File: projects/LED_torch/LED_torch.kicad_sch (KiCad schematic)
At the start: 4 parts, among them SW1 SW_DPDT_x2

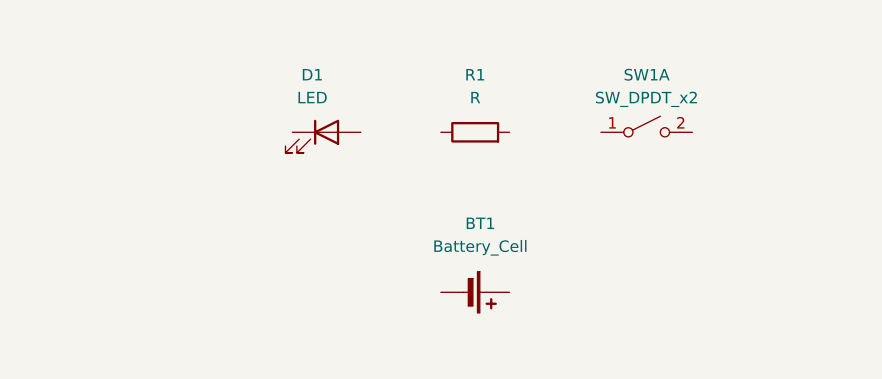
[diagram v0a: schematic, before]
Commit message: Project 1-LED Torch v01 v02 v03 and logos
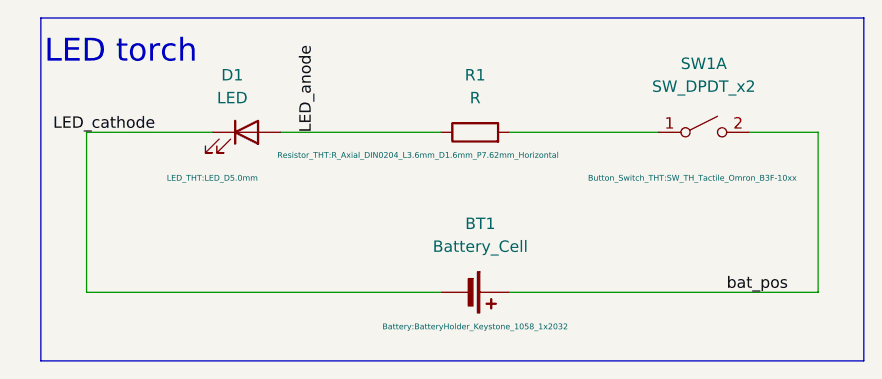
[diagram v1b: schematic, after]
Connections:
- net LED_anode: now reaches R1.1
- net LED_anode: now also D1.2 (A)
- net at R1.2: now also SW1.1 (A)
- net bat_pos: now reaches BT1.1 (+)
- net bat_pos: now also SW1.2 (B)
- net LED_cathode: now reaches BT1.2 (-)
- net LED_cathode: now also D1.1 (K)
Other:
- note added: "LED torch"
- moved on the sheet: D1, SW1A
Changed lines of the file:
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@@
 	(title_block
 		(title "LED Torch")
-		(date "2025-07-03")
+		(date "2025-07-05")
 		(rev "0.1")
 		(company "Sevillabot")
 		(comment 1 "Project 1 ")
 		(comment 2 "KiCAD like a Pro - Udemy Course")
-		(comment 3 "A basic PBC project")
+		(comment 3 "A basic PCB project")
+	)
+	(rectangle
+		(start 76.2 71.12)
+		(end 167.64 109.22)
+		(stroke
+			(width 0)
+			(type default)
+		)
+		(fill
+			(type none)
+		)
+	)
+	(text "LED torch"
+		(exclude_from_sim no)
+		(at 85.09 74.93 0)
+		(effects
+			(font
+				(face "Lato Black")
+				(size 2.54 2.54)
+			)
+		)
+	)
+	(wire
+		(pts
+			(xy 102.87 83.82) (xy 120.65 83.82)
+		)
+		(stroke
+			(width 0)
+			(type default)
+		)
+	)
+	(wire
+		(pts
+			(xy 81.28 83.82) (xy 95.25 83.82)
+		)
+		(stroke
+			(width 0)
+			(type default)
+		)
+	)
+	(wire
+		(pts
+			(xy 162.56 101.6) (xy 162.56 83.82)
+		)
+		(stroke
+			(width 0)
+			(type default)
+		)
+	)
+	(wire
+		(pts
+			(xy 128.27 83.82) (xy 144.78 83.82)
+		)
+		(stroke
+			(width 0)
+			(type default)
+		)
+	)
+	(wire
+		(pts
+			(xy 128.27 101.6) (xy 162.56 101.6)
+		)
+		(stroke
+			(width 0)
+			(type default)
+		)
+	)
+	(wire
+		(pts
+			(xy 162.56 83.82) (xy 154.94 83.82)
+		)
+		(stroke
+			(width 0)
+			(type default)
+		)
+	)
+	(wire
+		(pts
+			(xy 81.28 101.6) (xy 120.65 101.6)
+		)
+		(stroke
+			(width 0)
+			(type default)
+		)
+	)
+	(wire
+		(pts
+			(xy 81.28 83.82) (xy 81.28 101.6)
+		)
+		(stroke
+			(width 0)
+			(type default)
+		)
+	)
+	(label "LED_cathode"
+		(at 88.9 83.82 180)
+		(effects
+			(font
+				(size 1.27 1.27)
+			)
+			(justify right bottom)
+		)
+	)
+	(label "LED_anode"
+		(at 106.68 83.82 90)
+		(effects
+			(font
+				(size 1.27 1.27)
+			)
+			(justify left bottom)
+		)
+	)
+	(label "bat_pos"
+		(at 152.4 101.6 0)
+		(effects
+			(font
+				(size 1.27 1.27)
+			)
+			(justify left bottom)
+		)
 	)
 	(symbol
@@
 		(on_board yes)
 		(dnp no)
-		(fields_autoplaced yes)
 		(property "Reference" "R1"
 			(at 124.46 77.47 90)
@@
 		)
 		(property "Footprint" "Resistor_THT:R_Axial_DIN0204_L3.6mm_D1.6mm_P7.62mm_Horizontal"
-			(at 124.46 85.598 90)
-			(effects
-				(font
-					(size 1.27 1.27)
-				)
-				(hide yes)
+			(at 118.11 86.36 90)
+			(effects
+				(font
+					(face "Courier 10 Pitch")
+					(size 0.64 0.64)
+				)
 			)
 		)
@@
 		(on_board yes)
 		(dnp no)
-		(fields_autoplaced yes)
 		(property "Reference" "BT1"
 			(at 125.0315 93.98 90)
@@
 		)
 		(property "Footprint" "Battery:BatteryHolder_Keystone_1058_1x2032"
-			(at 124.714 101.6 90)
-			(effects
-				(font
-					(size 1.27 1.27)
-				)
-				(hide yes)
+			(at 124.46 105.41 90)
+			(effects
+				(font
+					(face "Courier 10 Pitch")
+					(size 0.64 0.64)
+				)
 			)
 		)
@@
 	(symbol
 		(lib_id "Switch:SW_DPST_x2")
-		(at 143.51 83.82 0)
+		(at 149.86 83.82 0)
 		(unit 1)
 		(exclude_from_sim no)
@@
 		(on_board yes)
 		(dnp no)
-		(fields_autoplaced yes)
 		(property "Reference" "SW1"
-			(at 143.51 77.47 0)
+			(at 149.86 76.2 0)
 			(effects
 				(font
@@
 		)
 		(property "Value" "SW_DPDT_x2"
-			(at 143.51 80.01 0)
+			(at 149.86 78.74 0)
 			(effects
 				(font
@@
 		)
 		(property "Footprint" "Button_Switch_THT:SW_TH_Tactile_Omron_B3F-10xx"
-			(at 143.51 83.82 0)
-			(effects
-				(font
-					(size 1.27 1.27)
-				)
-				(hide yes)
+			(at 148.59 88.9 0)
+			(effects
+				(font
+					(face "Courier 10 Pitch")
+					(size 0.64 0.64)
+				)
 			)
 		)
 		(property "Datasheet" "~"
-			(at 143.51 83.82 0)
+			(at 149.86 83.82 0)
 			(effects
 				(font
@@
 		)
 		(property "Description" "Single Pole Single Throw (SPST) switch, separate symbol"
-			(at 143.51 83.82 0)
+			(at 149.86 83.82 0)
 			(effects
 				(font
@@
 	(symbol
 		(lib_id "Device:LED")
-		(at 107.95 83.82 0)
+		(at 99.06 83.82 0)
 		(unit 1)
 		(exclude_from_sim no)
@@
 		(on_board yes)
 		(dnp no)
-		(fields_autoplaced yes)
 		(property "Reference" "D1"
-			(at 106.3625 77.47 0)
+			(at 97.4725 77.47 0)
 			(effects
 				(font
@@
 		)
 		(property "Value" "LED"
-			(at 106.3625 80.01 0)
+			(at 97.4725 80.01 0)
 			(effects
 				(font
@@
 		)
 		(property "Footprint" "LED_THT:LED_D5.0mm"
-			(at 107.95 83.82 0)
-			(effects
-				(font
-					(size 1.27 1.27)
-				)
-				(hide yes)
+			(at 95.25 88.9 0)
+			(effects
+				(font
+					(face "Courier 10 Pitch")
+					(size 0.64 0.64)
+				)
 			)
 		)
 		(property "Datasheet" "~"
-			(at 107.95 83.82 0)
+			(at 99.06 83.82 0)
 			(effects
 				(font
@@
 		)
 		(property "Description" "Light emitting diode"
-			(at 107.95 83.82 0)
+			(at 99.06 83.82 0)
 			(effects
 				(font
@@
 		)
 		(property "Sim.Pins" "1=K 2=A"
-			(at 107.95 83.82 0)
-			(effects
-				(font
+			(at 99.06 83.82 0)
+			(effects
+				(font

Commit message: Modify data on sheet box
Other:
- company: Sevillabot -> Manuel Heredia - Sevillabot
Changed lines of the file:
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@@
 	(title_block
 		(title "LED Torch")
-		(date "2025-07-05")
-		(rev "0.1")
-		(company "Sevillabot")
-		(comment 1 "Project 1 ")
-		(comment 2 "KiCAD like a Pro - Udemy Course")
-		(comment 3 "A basic PCB project")
+		(date "2025-07-23")
+		(rev "0.3")
+		(company "Manuel Heredia - Sevillabot")
+		(comment 1 "A basic PCB project of a LED torch")
+		(comment 2 "KiCAD like a Pro - Udemy Course (Project 1)")
 	)
 	(rectangle
